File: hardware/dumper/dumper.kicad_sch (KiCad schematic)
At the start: 15 parts

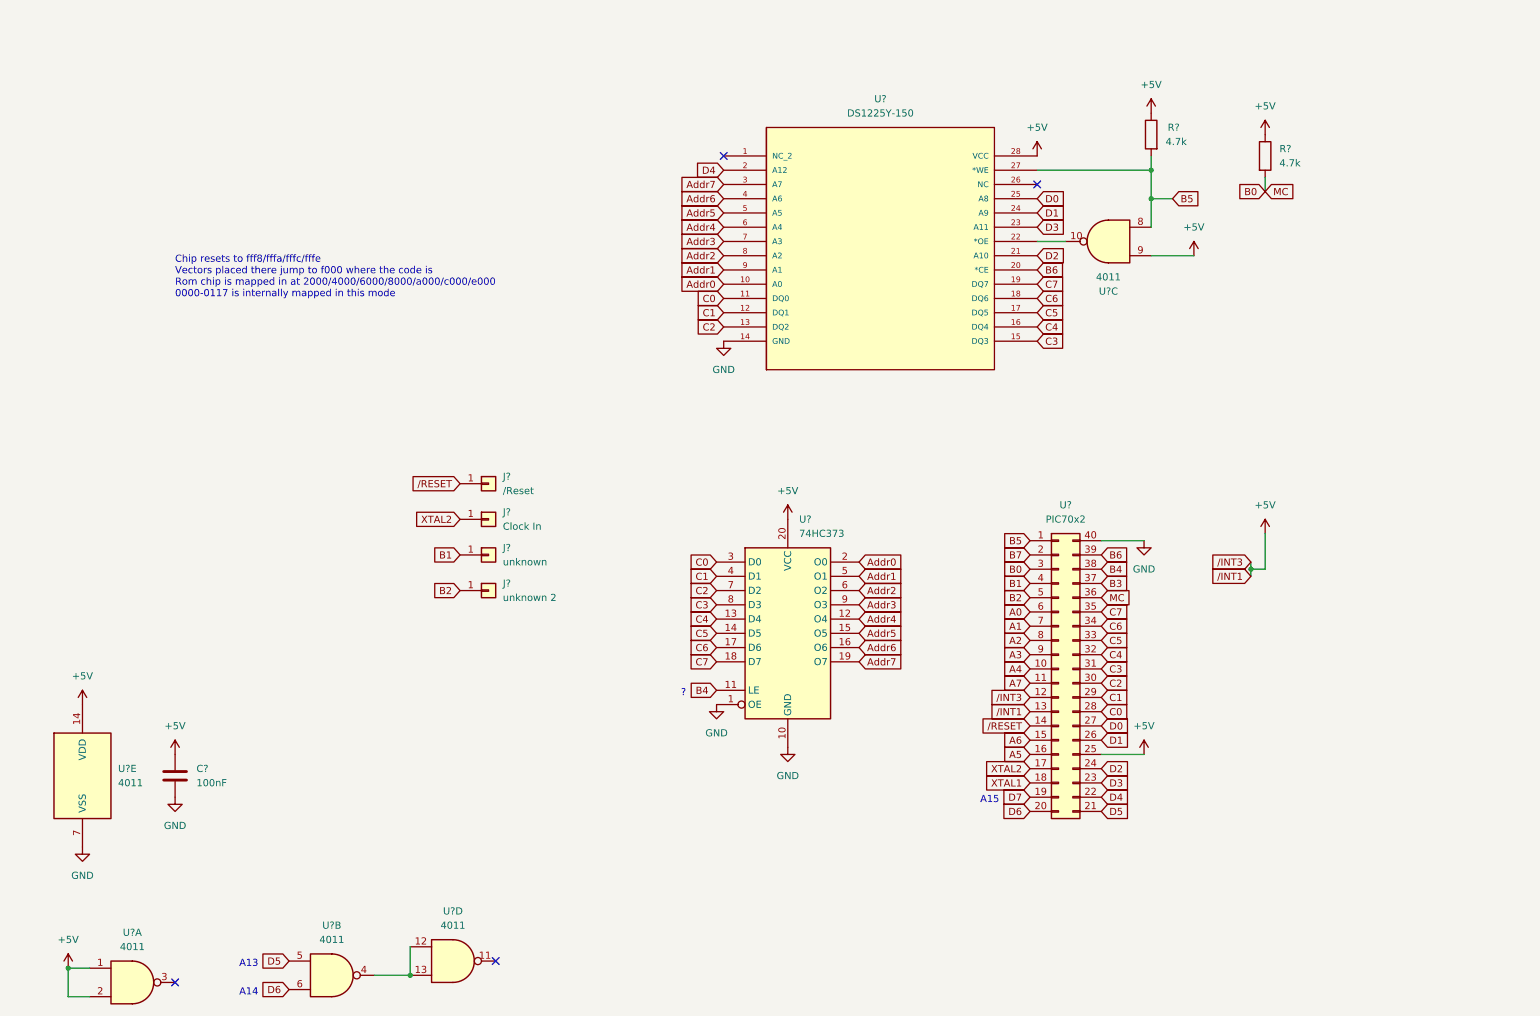
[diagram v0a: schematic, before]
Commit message: added board and tweaked schematic for EPROM variants
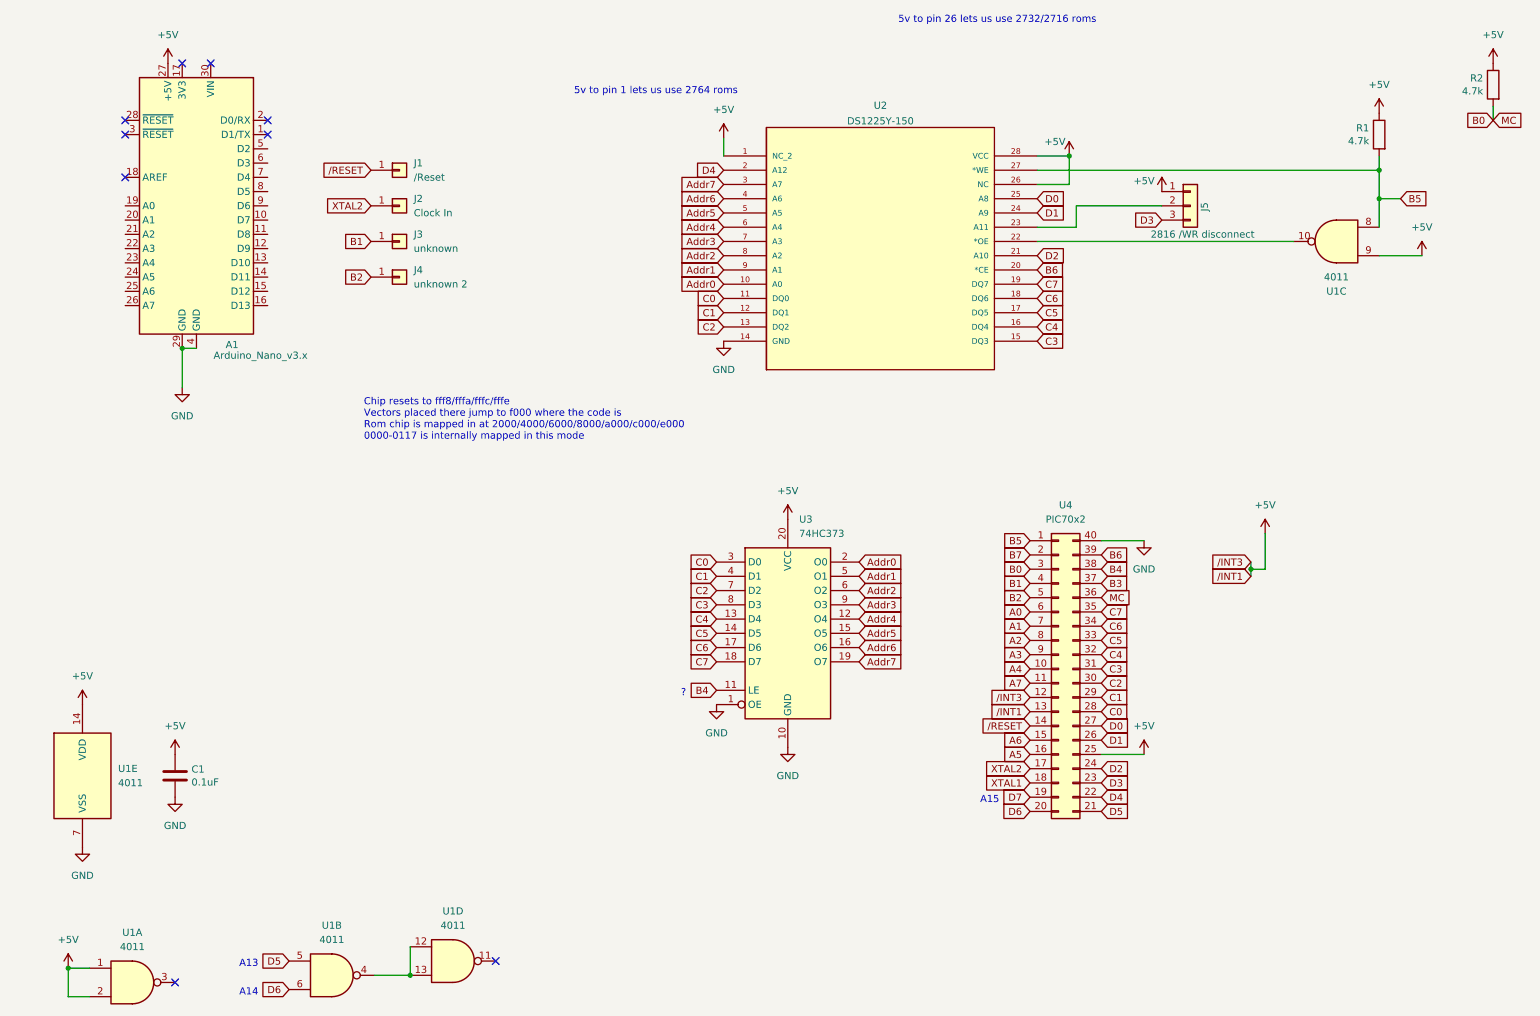
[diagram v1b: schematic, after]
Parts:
- removed C?: 100nF, symbol Device:C
- removed R? (x2): 4.7k, symbol Device:R
- added A1: Arduino_Nano_v3.x, Module:Arduino_Nano, symbol MCU_Module:Arduino_Nano_v3.x
- added C1: 0.1uF, Capacitor_THT:C_Axial_L3.8mm_D2.6mm_P7.50mm_Horizontal, symbol Device:C
- added J5: 2816 /WR disconnect, Connector_PinHeader_2.54mm:PinHeader_1x03_P2.54mm_Vertical, symbol Connector_Generic:Conn_01x03
- added R1, R2: 4.7k, Resistor_THT:R_Axial_DIN0207_L6.3mm_D2.5mm_P2.54mm_Vertical, symbol Device:R
- J1, J2, J3, J4: renamed from J?; footprint (none) -> Connector_PinHeader_2.54mm:PinHeader_1x01_P2.54mm_Vertical
- U1: renamed from U?; footprint (none) -> Package_DIP:DIP-14_W7.62mm
- U2: renamed from U?; footprint 21-0245A_28 -> Evan's misc parts:21-0245A_28
- U3: renamed from U?; footprint (none) -> Package_DIP:DIP-20_W7.62mm
- U4: renamed from U?; footprint (none) -> Package_DIP:DIP-40_W15.24mm
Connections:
- net +5V: now also U2.1 (NC_2), U2.26 (NC), A1.27 (+5V), C1.1, J5.1 (Pin_1), R1.1, R2.1
- net B0: now also R2.2
- net B5: now also R1.2
- net D3: now also J5.3 (Pin_3); no longer U2.23 (A11)
- net GND: now also A1.29 (GND), A1.4 (GND), C1.2
- new net: J5.2 (Pin_2), U2.23 (A11)
- no-connect marks 4 -> 9
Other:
- note added: "5v to pin 1 lets us use 2764 roms"
- note added: "5v to pin 26 lets us use 2732/2716 roms"
- moved on the sheet: J1, J2, J3, J4, U1C

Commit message: finished initial layout
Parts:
- added J10: arduino 10, Connector_PinHeader_2.54mm:PinHeader_1x01_P2.54mm_Vertical, symbol Connector_Generic:Conn_01x01
- added J11: ss, Connector_PinHeader_2.54mm:PinHeader_1x01_P2.54mm_Vertical, symbol Connector_Generic:Conn_01x01
- added J6: arduino 13, Connector_PinHeader_2.54mm:PinHeader_1x01_P2.54mm_Vertical, symbol Connector_Generic:Conn_01x01
- added J7: arduino 11, Connector_PinHeader_2.54mm:PinHeader_1x01_P2.54mm_Vertical, symbol Connector_Generic:Conn_01x01
- added J8: arduino 5, Connector_PinHeader_2.54mm:PinHeader_1x01_P2.54mm_Vertical, symbol Connector_Generic:Conn_01x01
- added J9: arduino 7, Connector_PinHeader_2.54mm:PinHeader_1x01_P2.54mm_Vertical, symbol Connector_Generic:Conn_01x01
- J3: value unknown -> data
- J4: value unknown 2 -> clock
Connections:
- net B1: now also A1.14 (D11), J7.1 (Pin_1)
- net B2: now also A1.16 (D13), J6.1 (Pin_1)
- net B3: now also A1.13 (D10), J10.1 (Pin_1), J11.1 (Pin_1)
- net XTAL2: now also A1.8 (D5), J8.1 (Pin_1)
- net /RESET: now also A1.10 (D7), J9.1 (Pin_1)
- no-connect marks 9 -> 24
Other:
- note added: "unused gates"
- moved on the sheet: A1, J1, J2, J3, J4

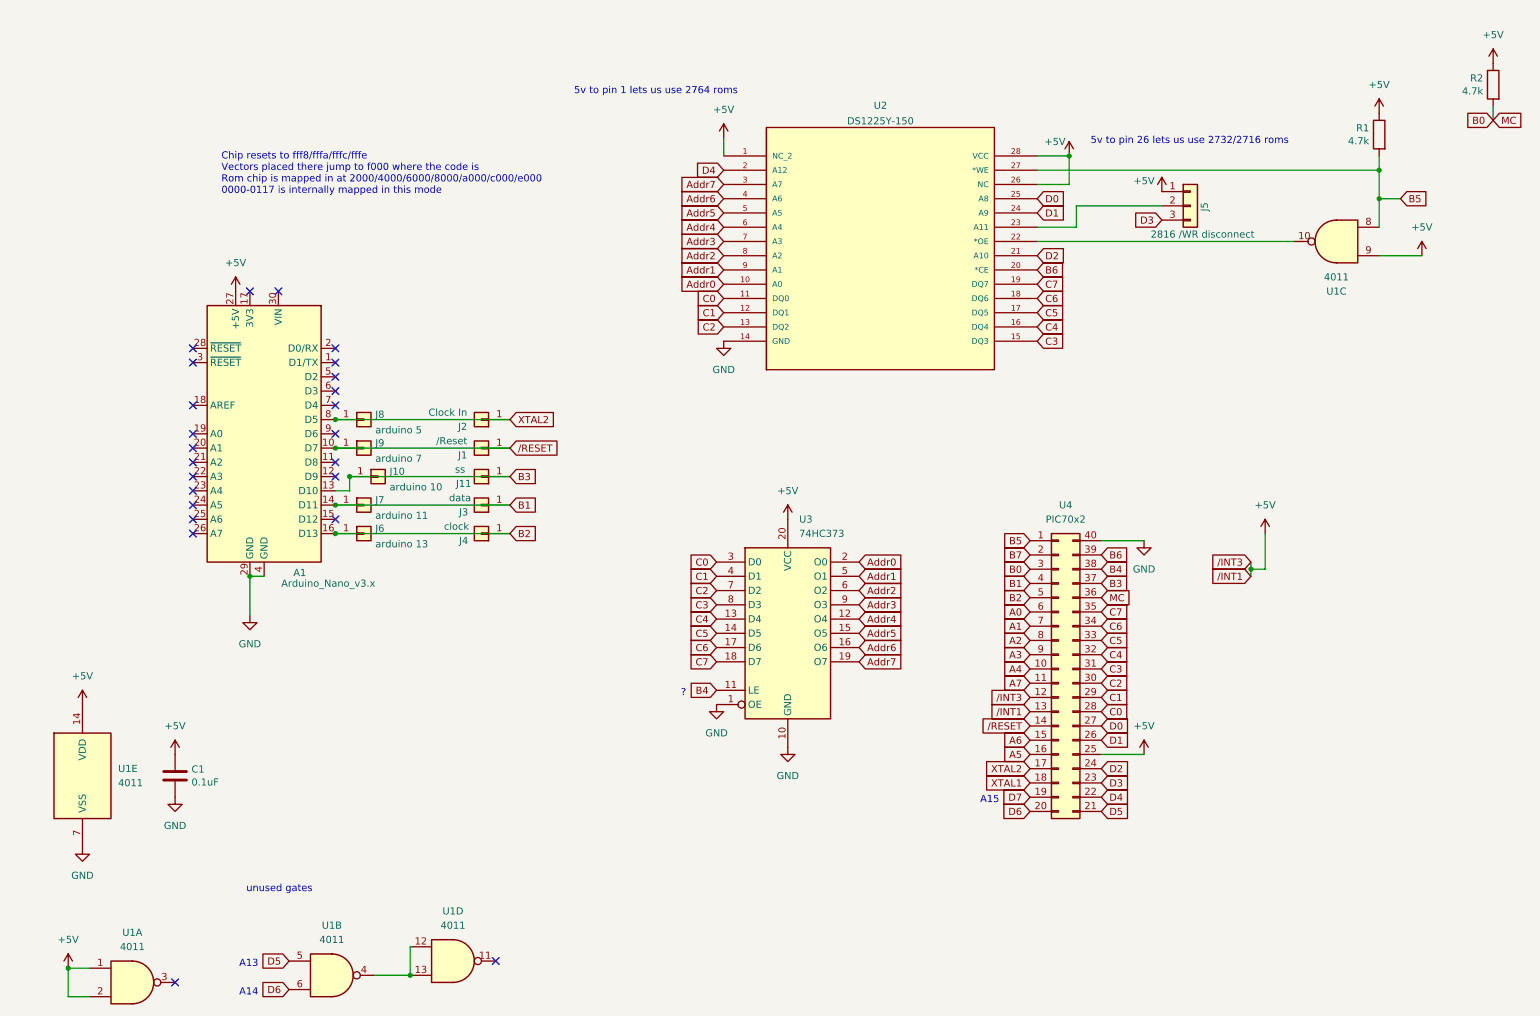
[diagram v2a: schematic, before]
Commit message: Simplified the schematic - no external writes needed
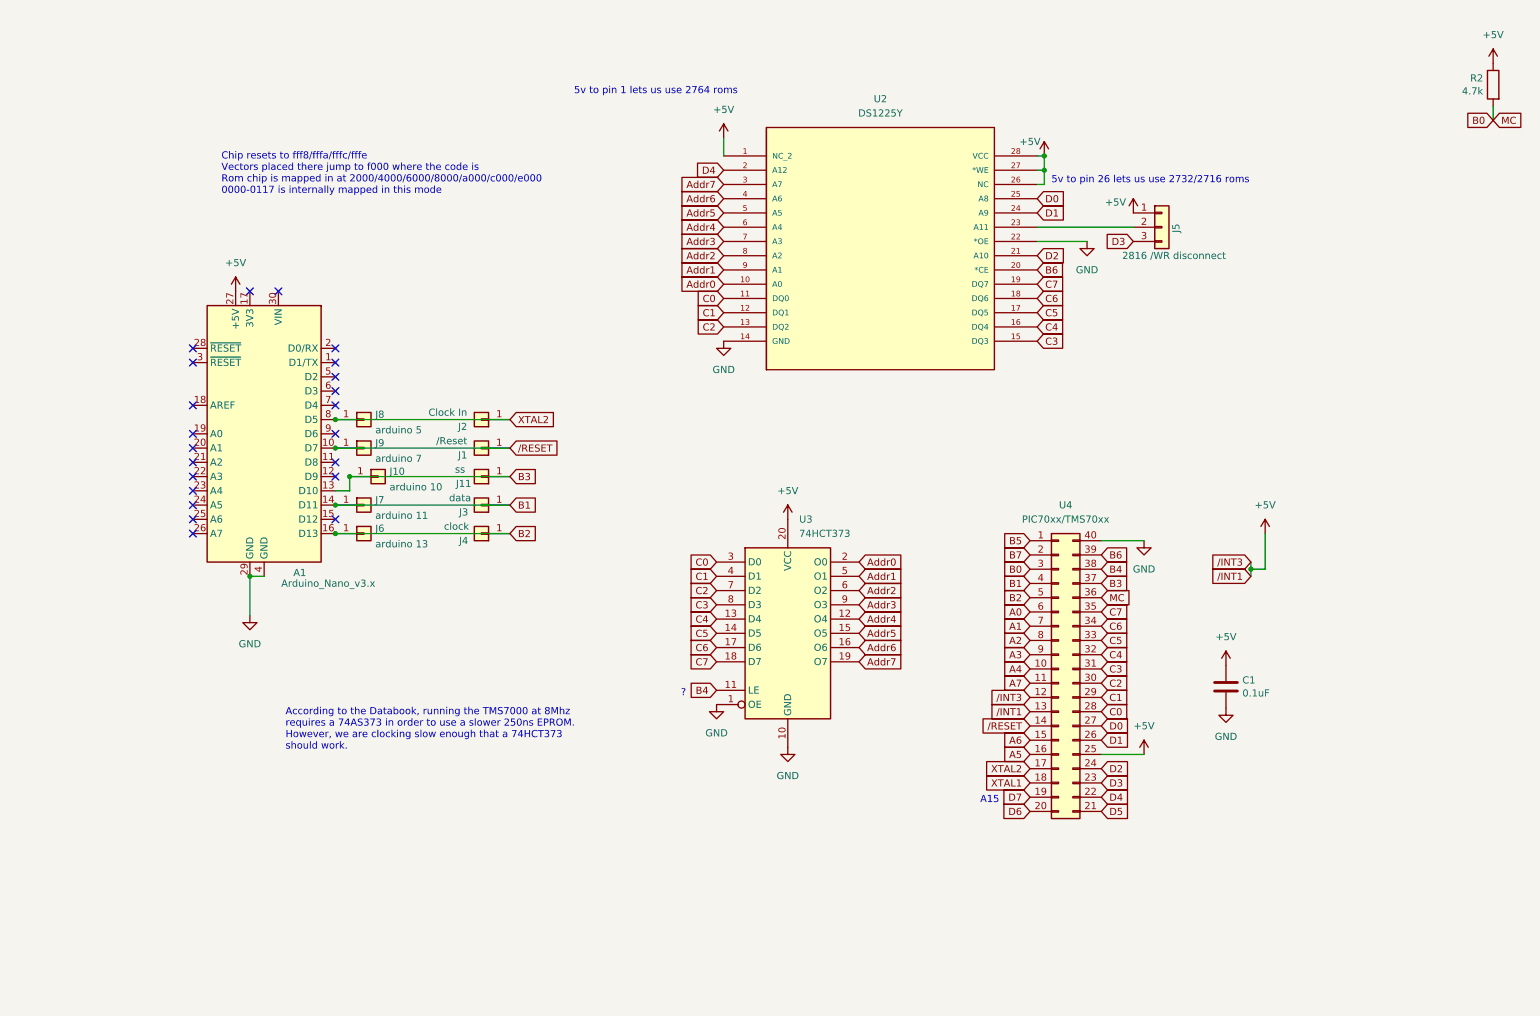
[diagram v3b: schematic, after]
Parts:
- removed R1: 4.7k, Resistor_THT:R_Axial_DIN0207_L6.3mm_D2.5mm_P2.54mm_Vertical, symbol Device:R
- removed U1: 4011, Package_DIP:DIP-14_W7.62mm, symbol 4xxx:4011
- U2: value DS1225Y-150 -> DS1225Y
- U3: value 74HC373 -> 74HCT373
- U4: value PIC70x2 -> PIC70xx/TMS70xx
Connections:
- net +5V: now also U2.27 (*WE)
- net B5: no longer U2.27 (*WE)
- net GND: now also U2.22 (*OE)
- no-connect marks 24 -> 22
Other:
- note added: "According to the Databook, running the TMS7000 at 8Mhz requires a 74AS373 in order to use a slower 250ns EPROM. However, we are clocking slow enough that a 74HCT373 should work."
- note removed: "A13"
- note removed: "A14"
- note removed: "unused gates"
- moved on the sheet: C1, J5

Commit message: updated board layout
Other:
- note removed: "?"
- moved on the sheet: R2
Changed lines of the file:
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@@
     (stroke (width 0) (type default) (color 0 0 0 0))
   )
-  (wire (pts (xy 276.86 33.02) (xy 276.86 30.48))
+  (wire (pts (xy 250.19 126.365) (xy 250.19 123.825))
     (stroke (width 0) (type default) (color 0 0 0 0))
   )
@@
     (effects (font (size 1.27 1.27)) (justify left bottom))
   )
-  (text "?" (at 132.08 135.89 0)
-    (effects (font (size 1.27 1.27)) (justify left bottom))
-  )
   (text "5v to pin 26 lets us use 2732/2716 roms" (at 198.12 44.45 0)
     (effects (font (size 1.27 1.27)) (justify left bottom))
@@
     )
   )
-  (global_label "MC" (shape input) (at 276.86 33.02 0) (fields_autoplaced)
-    (effects (font (size 1.27 1.27)) (justify left))
-    (property "Intersheet References" "${INTERSHEET_REFS}" (id 0) (at 281.9945 32.9406 0)
+  (global_label "MC" (shape input) (at 250.19 126.365 0) (fields_autoplaced)
+    (effects (font (size 1.27 1.27)) (justify left))
+    (property "Intersheet References" "${INTERSHEET_REFS}" (id 0) (at 255.3245 126.2856 0)
       (effects (font (size 1.27 1.27)) (justify left) hide)
     )
@@
     )
   )
-  (global_label "B0" (shape input) (at 276.86 33.02 180) (fields_autoplaced)
-    (effects (font (size 1.27 1.27)) (justify right))
-    (property "Intersheet References" "${INTERSHEET_REFS}" (id 0) (at 271.9674 32.9406 0)
+  (global_label "B0" (shape input) (at 250.19 126.365 180) (fields_autoplaced)
+    (effects (font (size 1.27 1.27)) (justify right))
+    (property "Intersheet References" "${INTERSHEET_REFS}" (id 0) (at 245.2974 126.2856 0)
       (effects (font (size 1.27 1.27)) (justify right) hide)
     )
@@
     )
   )
-  (symbol (lib_id "Device:R") (at 276.86 26.67 0) (mirror y) (unit 1)
+  (symbol (lib_id "Device:R") (at 250.19 120.015 0) (mirror y) (unit 1)
     (in_bom yes) (on_board yes)
-    (property "Reference" "R2" (id 0) (at 275.082 25.5016 0)
-      (effects (font (size 1.27 1.27)) (justify left))
-    )
-    (property "Value" "4.7k" (id 1) (at 275.082 27.813 0)
-      (effects (font (size 1.27 1.27)) (justify left))
-    )
-    (property "Footprint" "Resistor_THT:R_Axial_DIN0207_L6.3mm_D2.5mm_P2.54mm_Vertical" (id 2) (at 278.638 26.67 90)
-      (effects (font (size 1.27 1.27)) hide)
-    )
-    (property "Datasheet" "~" (id 3) (at 276.86 26.67 0)
+    (property "Reference" "R2" (id 0) (at 248.412 118.8466 0)
+      (effects (font (size 1.27 1.27)) (justify left))
+    )
+    (property "Value" "4.7k" (id 1) (at 248.412 121.158 0)
+      (effects (font (size 1.27 1.27)) (justify left))
+    )
+    (property "Footprint" "Resistor_THT:R_Axial_DIN0207_L6.3mm_D2.5mm_P2.54mm_Vertical" (id 2) (at 251.968 120.015 90)
+      (effects (font (size 1.27 1.27)) hide)
+    )
+    (property "Datasheet" "~" (id 3) (at 250.19 120.015 0)
       (effects (font (size 1.27 1.27)) hide)
     )
@@
     (pin "9")
   )
-  (symbol (lib_id "power:+5V") (at 276.86 22.86 0) (unit 1)
-    (in_bom yes) (on_board yes) (fields_autoplaced)
-    (property "Reference" "#PWR0118" (id 0) (at 276.86 26.67 0)
-      (effects (font (size 1.27 1.27)) hide)
-    )
-    (property "Value" "+5V" (id 1) (at 276.86 17.78 0))
-    (property "Footprint" "" (id 2) (at 276.86 22.86 0)
-      (effects (font (size 1.27 1.27)) hide)
-    )
-    (property "Datasheet" "" (id 3) (at 276.86 22.86 0)
-      (effects (font (size 1.27 1.27)) hide)
-    )
+  (symbol (lib_id "power:+5V") (at 250.19 116.205 0) (unit 1)
+    (in_bom yes) (on_board yes) (fields_autoplaced)
+    (property "Reference" "#PWR0118" (id 0) (at 250.19 120.015 0)
+      (effects (font (size 1.27 1.27)) hide)
+    )
+    (property "Value" "+5V" (id 1) (at 250.19 111.125 0))
+    (property "Footprint" "" (id 2) (at 250.19 116.205 0)
+      (effects (font (size 1.27 1.27)) hide)
+    )
+    (property "Datasheet" "" (id 3) (at 250.19 116.205 0)
+      (effects (font (size 1.27 1.27)) hide)
+    )
